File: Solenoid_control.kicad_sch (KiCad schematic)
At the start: 10 parts, among them U23 RSCD06D3

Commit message: VER1.0: сделал все питание и один измерительный канал
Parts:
- J24: footprint Connector_My:Mini-Fit_01x02_Vertical -> Connector_Molex:Molex_Mini-Fit_Jr_5569-02A2_2x01_P4.20mm_Horizontal
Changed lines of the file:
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@@
 			)
 		)
-		(property "Footprint" "Connector_My:Mini-Fit_01x02_Vertical"
+		(property "Footprint" "Connector_Molex:Molex_Mini-Fit_Jr_5569-02A2_2x01_P4.20mm_Horizontal"
 			(at 184.15 101.6 0)
 			(hide yes)

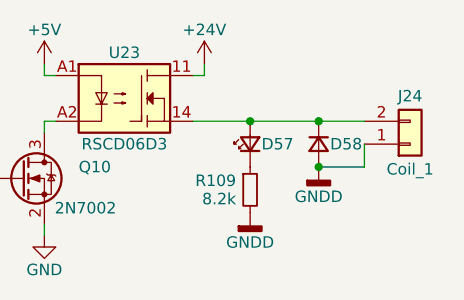
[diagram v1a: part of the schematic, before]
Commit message: VER1.0: развел все кроме ножек МК
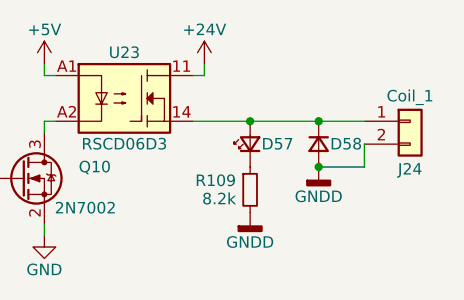
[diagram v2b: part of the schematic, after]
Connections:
- net GNDD: now also J24.2 (Pin_2); no longer J24.1 (Pin_1)
- net at D57.2 (A), D58.1 (K), U23.14: now also J24.1 (Pin_1); no longer J24.2 (Pin_2)
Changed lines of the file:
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@@
 	(symbol
 		(lib_id "Connector_Generic:Conn_01x02")
-		(at 184.15 101.6 0)
-		(mirror x)
+		(at 184.15 99.06 0)
 		(unit 1)
 		(body_style 1)
@@
 		(dnp no)
 		(property "Reference" "J24"
-			(at 184.15 96.266 0)
+			(at 184.15 104.394 0)
 			(show_name no)
 			(do_not_autoplace no)
@@
 		)
 		(property "Value" ""
-			(at 186.69 99.06 0)
+			(at 186.69 101.6 0)
 			(hide yes)
 			(show_name no)
@@
 		)
 		(property "Footprint" "Connector_Molex:Molex_Mini-Fit_Jr_5569-02A2_2x01_P4.20mm_Horizontal"
-			(at 184.15 101.6 0)
+			(at 184.15 99.06 0)
 			(hide yes)
 			(show_name no)
@@
 		)
 		(property "Datasheet" ""
-			(at 184.15 101.6 0)
+			(at 184.15 99.06 0)
 			(hide yes)
 			(show_name no)
@@
 		)
 		(property "Description" "Generic connector, single row, 01x02, script generated (kicad-library-utils/schlib/autogen/connector/)"
-			(at 184.15 101.6 0)
+			(at 184.15 99.06 0)
 			(hide yes)
 			(show_name no)
@@
 		)
 		(property "Replacement" ""
-			(at 184.15 101.6 0)
+			(at 184.15 99.06 0)
 			(hide yes)
 			(show_name no)
@@
 		)
 		(property "Purpose" "Coil_1"
-			(at 184.15 104.394 0)
+			(at 184.15 96.266 0)
 			(show_name no)
 			(do_not_autoplace no)
@@
 		)
 		(property "Description P/N" "Connector"
-			(at 184.15 101.6 0)
+			(at 184.15 99.06 0)
 			(hide yes)
 			(show_name no)
@@
 		)
 		(property "Product Name" "DS1073-01-2x1-MVT6"
-			(at 184.15 101.6 0)
+			(at 184.15 99.06 0)
 			(hide yes)
 			(show_name no)

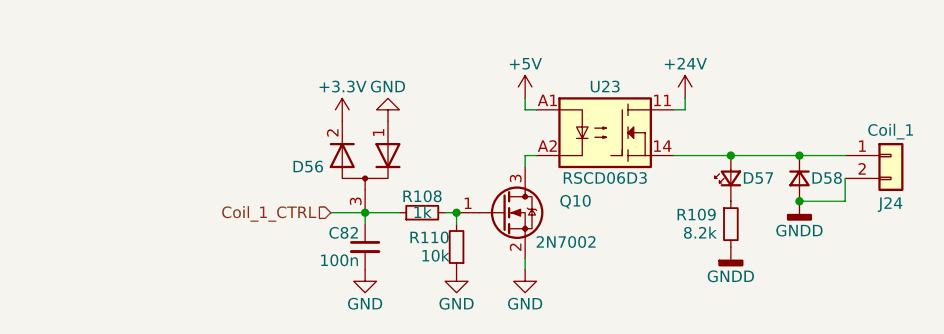
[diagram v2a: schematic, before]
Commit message: VER1.0: добавил предохранители каждому клапану и отдельно по питанию
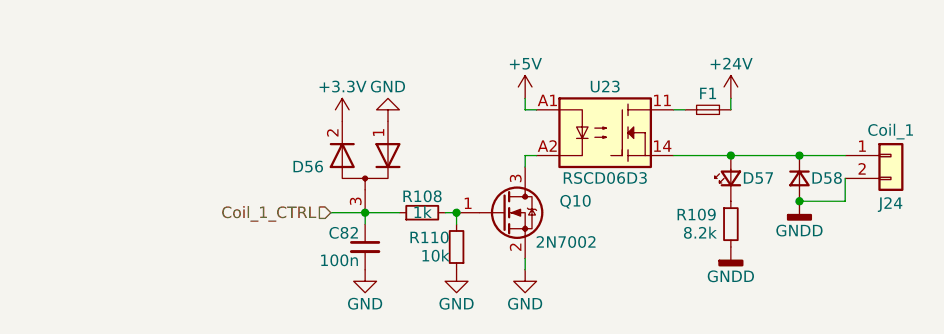
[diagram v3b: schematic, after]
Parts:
- added F1: MF-SM075/60-2, Fuse:Fuse_Bourns_MF-SM_7.98x5.44mm, symbol Device:Fuse_Small
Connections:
- net +24V: now also F1.2; no longer U23.11
- new net: F1.1, U23.11
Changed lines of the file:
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@@
 	(wire
 		(pts
-			(xy 161.29 92.71) (xy 161.29 93.98)
+			(xy 166.37 92.71) (xy 166.37 93.98)
 		)
 		(stroke
@@
 		(lib_name "+24V_1")
 		(lib_id "power:+24V")
-		(at 161.29 92.71 0)
+		(at 166.37 92.71 0)
 		(mirror y)
 		(unit 1)
@@
 		(dnp no)
 		(property "Reference" "#PWR0276"
-			(at 161.29 96.52 0)
+			(at 166.37 96.52 0)
 			(hide yes)
 			(show_name no)
@@
 		)
 		(property "Value" "+24V"
-			(at 161.29 88.9 0)
+			(at 166.37 88.9 0)
 			(show_name no)
 			(do_not_autoplace no)
@@
 		)
 		(property "Footprint" ""
-			(at 161.29 92.71 0)
+			(at 166.37 92.71 0)
 			(hide yes)
 			(show_name no)
@@
 		)
 		(property "Datasheet" ""
-			(at 161.29 92.71 0)
+			(at 166.37 92.71 0)
 			(hide yes)
 			(show_name no)
@@
 		)
 		(property "Description" "Power symbol creates a global label with name \"+24V\""
-			(at 161.29 92.71 0)
+			(at 166.37 92.71 0)
 			(hide yes)
 			(show_name no)
@@
 					(unit 1)
 				)
+			)
+		)
+	)
+	(symbol
+		(lib_id "Device:Fuse_Small")
+		(at 163.83 93.98 0)
+		(mirror x)
+		(unit 1)
+		(body_style 1)
+		(exclude_from_sim no)
+		(in_bom yes)
+		(on_board yes)
+		(in_pos_files yes)
+		(dnp no)
+		(property "Reference" "F1"
+			(at 163.83 92.202 0)
+			(show_name no)
+			(do_not_autoplace no)
+			(effects
+				(font
+					(size 1.27 1.27)
+				)
+			)
+		)
+		(property "Value" "MF-SM075/60-2"
+			(at 163.83 91.44 0)
+			(hide yes)
+			(show_name no)
+			(do_not_autoplace no)
+			(effects
+				(font
+					(size 1.27 1.27)
+				)
+			)
+		)
+		(property "Footprint" "Fuse:Fuse_Bourns_MF-SM_7.98x5.44mm"
+			(at 163.83 93.98 0)
+			(hide yes)
+			(show_name no)
+			(do_not_autoplace no)
+			(effects
+				(font
+					(size 1.27 1.27)
+				)
+			)
+		)
+		(property "Datasheet" ""
+			(at 163.83 93.98 0)
+			(hide yes)
+			(show_name no)
+			(do_not_autoplace no)
+			(effects
+				(font
+					(size 1.27 1.27)
+				)
+			)
+		)
+		(property "Description" "Fuse, small symbol"
+			(at 163.83 93.98 0)
+			(hide yes)
+			(show_name no)
+			(do_not_autoplace no)
+			(effects
+				(font
+					(size 1.27 1.27)
+				)
+			)
+		)
+		(pin "2"
+		)
+		(pin "1"
+		)
+		(instances
+			(project "Storage_Armature_MCU_PCB"
+				(path "/7b040528-7065-4d6b-8722-075d9f593d01/23b1d26d-0438-4c0a-ba0f-8a73a3aee4c0"
+					(reference "F1")
+					(unit 1)
+				)
+				(path "/7b040528-7065-4d6b-8722-075d9f593d01/7474189f-61b5-451d-98c9-7dd492ce5d9c"
+					(reference "F4")
+					(unit 1)
+				)
+				(path "/7b040528-7065-4d6b-8722-075d9f593d01/a3641e02-0c05-4204-9bda-a076fe6b4dee"
+					(reference "F5")
+					(unit 1)
+				)
+				(path "/7b040528-7065-4d6b-8722-075d9f593d01/f2e4ada1-f365-47a5-a07e-bc132ee8c231"
+					(reference "F6")
+					(unit 1)
+				)

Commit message: VER1.0: добавил светодиоды, тестпоинты и мягкий старт 24В
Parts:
- added D68: (no value), LED_SMD:LED_0805_2012Metric, symbol Device:LED_Small
- added R120: 1k, Resistor_SMD:R_0805_2012Metric_Pad1.20x1.40mm_HandSolder, symbol Device:R_Small
- C82: value 100n -> 10n
- R109: value 8.2k -> 4.7k
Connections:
- net +5V: now also D68.2 (A)
- net Coil_1_CTRL: no longer C82.1
- net at Q10.3 (D), U23.A2: now also R120.2
- net at Q10.1 (G), R108.2, R110.2: now also C82.1
- new net: D68.1 (K), R120.1
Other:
- moved on the sheet: C82, D56, R108, R110

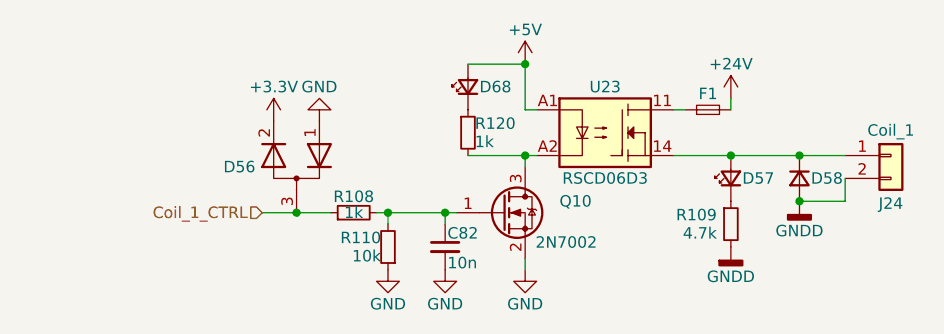
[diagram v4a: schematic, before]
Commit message: VER1.0: добавил RS485, Board ID, вырезы в плате
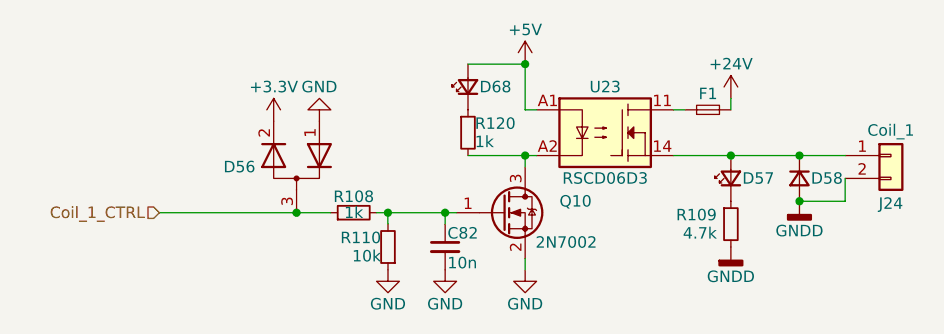
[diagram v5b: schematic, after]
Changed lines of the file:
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@@
+	)
+	(junction
+		(at 143.51 88.9)
+		(diameter 0)
+		(color 0 0 0 0)
+	)
+	(junction
+		(at 173.99 99.06)
+		(diameter 0)
+		(color 0 0 0 0)
 	)
 	(junction
@@
 		(color 0 0 0 0)
 	)
-	(junction
-		(at 143.51 88.9)
-		(diameter 0)
-		(color 0 0 0 0)
-	)
-	(junction
-		(at 173.99 99.06)
-		(diameter 0)
-		(color 0 0 0 0)
-	)
 	(wire
 		(pts
@@
 	(wire
 		(pts
+			(xy 102.87 105.41) (xy 118.11 105.41)
+		)
+		(stroke
+			(width 0)
+			(type default)
+		)
+	)
+	(wire
+		(pts
 			(xy 166.37 92.71) (xy 166.37 93.98)
 		)
@@
 		(pts
 			(xy 128.27 105.41) (xy 128.27 106.68)
-		)
-		(stroke
-			(width 0)
-			(type default)
-		)
-	)
-	(wire
-		(pts
-			(xy 114.3 105.41) (xy 118.11 105.41)
 		)
 		(stroke
@@
 	(hierarchical_label "Coil_1_CTRL"
 		(shape input)
-		(at 114.3 105.41 180)
+		(at 102.87 105.41 180)
 		(effects
 			(font
